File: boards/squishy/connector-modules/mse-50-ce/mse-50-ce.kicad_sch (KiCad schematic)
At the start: 14 parts, among them J1 SCSI PHY Mezz, J3 Conn_01x04, J5 Centronics 50, U1 M24C02-RMC

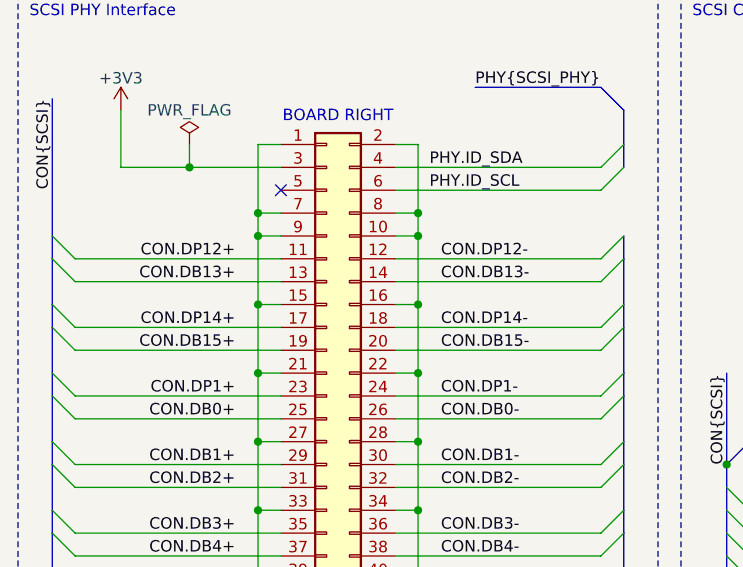
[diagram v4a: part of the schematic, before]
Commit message: squishy: connectors: s/DP12/DB12/g s/DP14/DB14/g
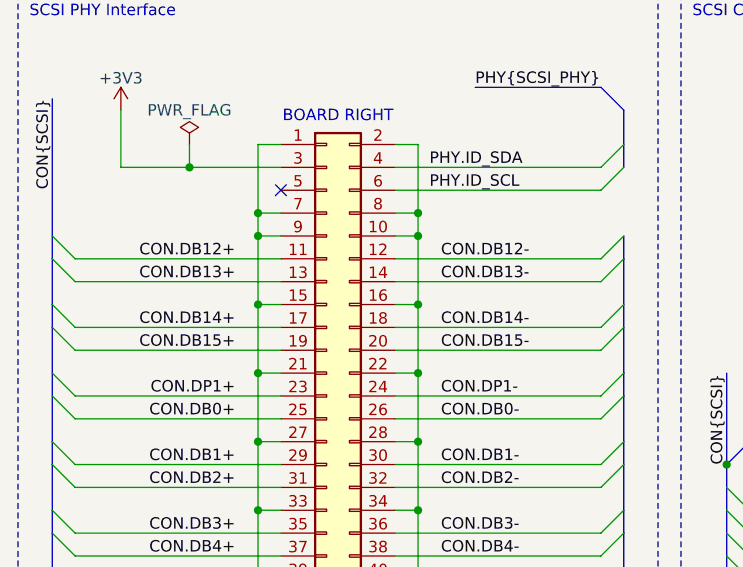
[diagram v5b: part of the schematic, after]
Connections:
- net CON.DP12+ renamed CON.DB12+
- net CON.DP12- renamed CON.DB12-
- net CON.DP14+ renamed CON.DB14+
- net CON.DP14- renamed CON.DB14-
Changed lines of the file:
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@@
 		)
 	)
-	(label "CON.DP14-"
+	(label "CON.DB14-"
 		(at 60.96 52.07 0)
 		(fields_autoplaced yes)
@@
 		)
 	)
-	(label "CON.DP12+"
+	(label "CON.DB12+"
 		(at 38.1 44.45 180)
 		(fields_autoplaced yes)
@@
 		)
 	)
-	(label "CON.DP12-"
+	(label "CON.DB12-"
 		(at 60.96 44.45 0)
 		(fields_autoplaced yes)
@@
 		)
 	)
-	(label "CON.DP14+"
+	(label "CON.DB14+"
 		(at 38.1 52.07 180)
 		(fields_autoplaced yes)

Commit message: squishy: connectors: updated SCSI connector metadata for mse-50-ce
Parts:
- J5: value Centronics 50 -> 112-050-213R001; MFR (none) -> NorComp; MPN (none) -> 112-050-213R001; URL (none) -> https://www.norcomp.net/series/112-series?search_part=112-0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
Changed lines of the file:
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@@
 			)
 		)
-		(property "Value" "Centronics 50"
-			(at 123.19 67.31 0)
+		(property "Value" "112-050-213R001"
+			(at 123.19 101.6 90)
 			(effects
 				(font
@@
 			)
 		)
-		(property "Datasheet" "~"
+		(property "Datasheet" "https://content.norcomp.net/rohspdfs/SCSI-050Ribbon/11Y/112/112-YYY-213RYY1.pdf"
 			(at 121.92 120.65 0)
 			(effects
@@
 			)
 		)
-		(property "Description" "Generic connector, double row, 02x25, counter clockwise pin numbering scheme (similar to DIP package numbering), with shielding"
+		(property "Description" "Centronics 50-pin Connector"
 			(at 123.19 101.6 0)
 			(effects
+				(font
+					(size 1.27 1.27)
+				)
+				(hide yes)
+			)
+		)
+		(property "MFR" "NorComp"
+			(at 123.19 101.6 0)
+			(effects
+				(font
+					(size 1.27 1.27)
+				)
+				(hide yes)
+			)
+		)
+		(property "MPN" "112-050-213R001"
+			(at 123.19 101.6 0)
+			(effects
+				(font
+					(size 1.27 1.27)
+				)
+				(hide yes)
+			)
+		)
+		(property "URL" "https://www.norcomp.net/series/112-series?search_part=112-050-213R001"
+			(at 123.19 101.6 0)
+			(effects

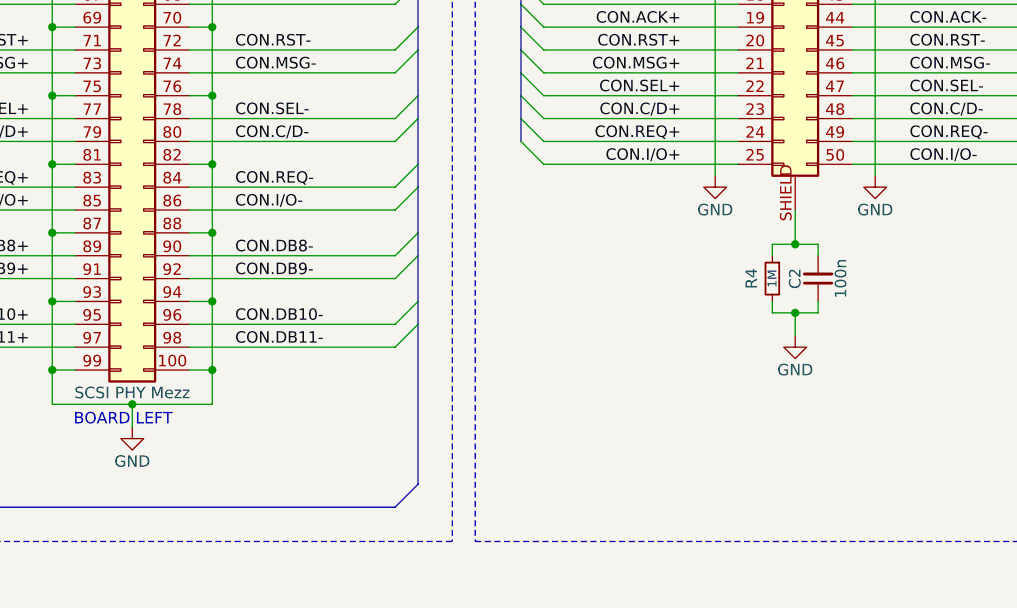
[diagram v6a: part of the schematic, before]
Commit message: squishy: connectors: cleaned up ERC on the mse-50-ce connector
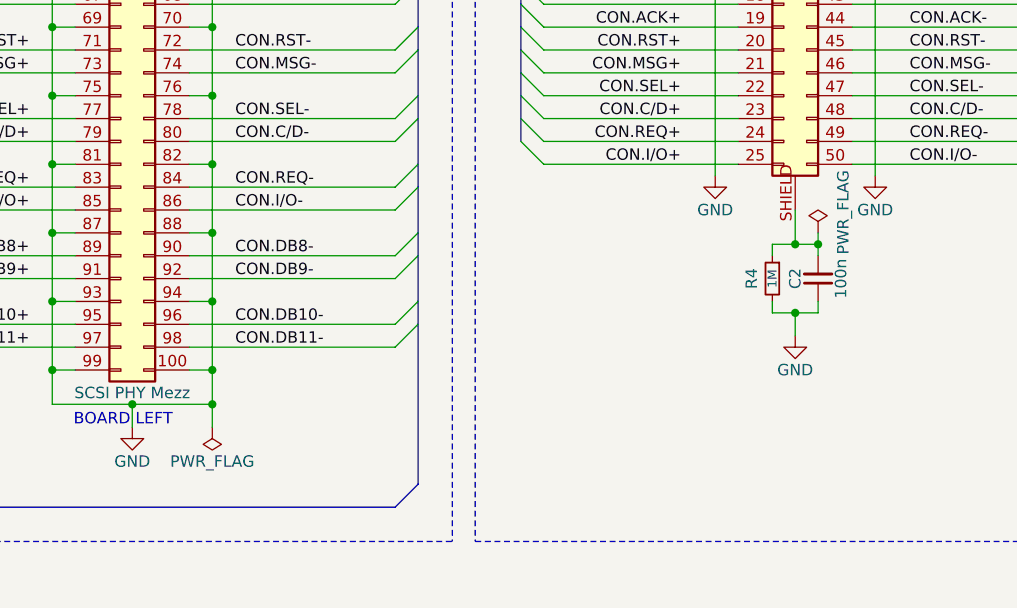
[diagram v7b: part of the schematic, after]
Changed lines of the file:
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@@
 	)
 	(junction
+		(at 125.73 142.24)
+		(diameter 0)
+		(color 0 0 0 0)
+	)
+	(junction
+		(at 58.42 160.02)
+		(diameter 0)
+		(color 0 0 0 0)
+	)
+	(junction
 		(at 58.42 41.91)
 		(diameter 0)
@@
 	(wire
 		(pts
+			(xy 125.73 140.97) (xy 125.73 142.24)
+		)
+		(stroke
+			(width 0)
+			(type default)
+		)
+	)
+	(wire
+		(pts
 			(xy 55.88 133.35) (xy 58.42 133.35)
 		)
@@
 	(wire
 		(pts
+			(xy 58.42 160.02) (xy 58.42 162.56)
+		)
+		(stroke
+			(width 0)
+			(type default)
+		)
+	)
+	(wire
+		(pts
 			(xy 40.64 57.15) (xy 40.64 64.77)
 		)
@@
 	)
 	(symbol
+		(lib_id "power:PWR_FLAG")
+		(at 58.42 162.56 180)
+		(unit 1)
+		(exclude_from_sim no)
+		(in_bom yes)
+		(on_board yes)
+		(dnp no)
+		(property "Reference" "#FLG02"
+			(at 58.42 164.465 0)
+			(effects
+				(font
+					(size 1.27 1.27)
+				)
+				(hide yes)
+			)
+		)
+		(property "Value" "PWR_FLAG"
+			(at 58.42 166.37 0)
+			(effects
+				(font
+					(size 1.27 1.27)
+				)
+			)
+		)
+		(property "Footprint" ""
+			(at 58.42 162.56 0)
+			(effects
+				(font
+					(size 1.27 1.27)
+				)
+				(hide yes)
+			)
+		)
+		(property "Datasheet" "~"
+			(at 58.42 162.56 0)
+			(effects
+				(font
+					(size 1.27 1.27)
+				)
+				(hide yes)
+			)
+		)
+		(property "Description" "Special symbol for telling ERC where power comes from"
+			(at 58.42 162.56 0)
+			(effects
+				(font
+					(size 1.27 1.27)
+				)
+				(hide yes)
+			)
+		)
+		(pin "1"
+		)
+		(instances
+			(project "mse-50-ce"
+				(path "/bd9eafec-5355-49e4-b2e3-916daacb0a86"
+					(reference "#FLG02")
+					(unit 1)
+				)
+			)
+		)
+	)
+	(symbol
 		(lib_id "power:GND")
 		(at 123.19 152.4 0)
@@
 					(unit 1)
 				)
+			)
+		)
+	)
+	(symbol
+		(lib_id "power:PWR_FLAG")
+		(at 125.73 140.97 0)
+		(unit 1)
+		(exclude_from_sim no)
+		(in_bom yes)
+		(on_board yes)
+		(dnp no)
+		(property "Reference" "#FLG03"
+			(at 125.73 139.065 0)
+			(effects
+				(font
+					(size 1.27 1.27)
+				)
+				(hide yes)
+			)
+		)
+		(property "Value" "PWR_FLAG"
+			(at 128.524 138.684 90)
+			(effects
+				(font
+					(size 1.27 1.27)
+				)
+			)
+		)
+		(property "Footprint" ""
+			(at 125.73 140.97 0)
+			(effects
+				(font
+					(size 1.27 1.27)
+				)
+				(hide yes)
+			)
+		)
+		(property "Datasheet" "~"
+			(at 125.73 140.97 0)
+			(effects
+				(font
+					(size 1.27 1.27)
+				)
+				(hide yes)
+			)
+		)
+		(property "Description" "Special symbol for telling ERC where power comes from"
+			(at 125.73 140.97 0)
+			(effects
+				(font
+					(size 1.27 1.27)
+				)
+				(hide yes)
+			)
+		)
+		(pin "1"
+		)
+		(instances
+			(project "mse-50-ce"
+				(path "/bd9eafec-5355-49e4-b2e3-916daacb0a86"
+					(reference "#FLG03")
+					(unit 1)
+				)

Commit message: squishy: connectors: updated part metadata on mse-50-ce prior to CAM generation
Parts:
- J3: now left out of the parts list
- J5: SUPPLIER (none) -> DigiKey; SUPPLIER_OC (none) -> 1050RFA-ND; SUPPLIER_URL (none) -> https://www.digikey.com/short/vt4vc8rp
- R4: MFR (none) -> Vishay Dale; MPN (none) -> CRCW06031M00FKEA; SUPPLIER_OC (none) -> 541-1.00MHDKR-ND; SUPPLIER_URL (none) -> https://www.digikey.com/short/18qqp0zw; Tolerance (none) -> ±1% 1/10W
- U1: MFR (none) -> STMicroelectronics; MPN (none) -> M24C02-RMC6TG; SUPPLIER (none) -> DigiKey; SUPPLIER_OC (none) -> 497-17822-1-ND; SUPPLIER_URL (none) -> https://www.digikey.com/short/r9drrzr3
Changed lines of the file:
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@@
 			)
 		)
-		(property "Datasheet" ""
+		(property "Datasheet" "https://www.vishay.com/docs/20035/dcrcwe3.pdf"
 			(at 120.65 146.05 0)
 			(effects
@@
 			)
 		)
-		(property "MFR" ""
+		(property "MFR" "Vishay Dale"
 			(at 120.65 146.05 90)
 			(effects
@@
 			)
 		)
-		(property "MPN" ""
+		(property "MPN" "CRCW06031M00FKEA"
 			(at 120.65 146.05 90)
 			(effects
@@
 			)
 		)
-		(property "Tolerance" ""
+		(property "Tolerance" "±1% 1/10W"
 			(at 120.65 146.05 0)
 			(effects
@@
 			)
 		)
-		(property "SUPPLIER_OC" ""
+		(property "SUPPLIER_OC" "541-1.00MHDKR-ND"
 			(at 120.65 146.05 0)
 			(effects
@@
 			)
 		)
-		(property "SUPPLIER_URL" ""
+		(property "SUPPLIER_URL" "https://www.digikey.com/short/18qqp0zw"
 			(at 120.65 146.05 0)
 			(effects
@@
 		(unit 1)
 		(exclude_from_sim no)
-		(in_bom yes)
+		(in_bom no)
 		(on_board yes)
 		(dnp no)
@@
 		)
 		(property "URL" "https://www.norcomp.net/series/112-series?search_part=112-050-213R001"
+			(at 123.19 101.6 0)
+			(effects
+				(font
+					(size 1.27 1.27)
+				)
+				(hide yes)
+			)
+		)
+		(property "SUPPLIER" "DigiKey"
+			(at 123.19 101.6 0)
+			(effects
+				(font
+					(size 1.27 1.27)
+				)
+				(hide yes)
+			)
+		)
+		(property "SUPPLIER_OC" "1050RFA-ND"
+			(at 123.19 101.6 0)
+			(effects
+				(font
+					(size 1.27 1.27)
+				)
+				(hide yes)
+			)
+		)
+		(property "SUPPLIER_URL" "https://www.digikey.com/short/vt4vc8rp"
 			(at 123.19 101.6 0)
 			(effects
@@
 			(at 238.76 147.32 0)
 			(effects
+				(font
+					(size 1.27 1.27)
+				)
+				(hide yes)
+			)
+		)
+		(property "MFR" "STMicroelectronics"
+			(at 238.76 147.32 0)
+			(effects
+				(font
+					(size 1.27 1.27)
+				)
+				(hide yes)
+			)
+		)
+		(property "MPN" "M24C02-RMC6TG"
+			(at 238.76 147.32 0)
+			(effects
+				(font
+					(size 1.27 1.27)
+				)
+				(hide yes)
+			)
+		)
+		(property "SUPPLIER" "DigiKey"
+			(at 238.76 147.32 0)
+			(effects
+				(font
+					(size 1.27 1.27)
+				)
+				(hide yes)
+			)
+		)
+		(property "SUPPLIER_OC" "497-17822-1-ND"
+			(at 238.76 147.32 0)
+			(effects
+				(font
+					(size 1.27 1.27)
+				)
+				(hide yes)
+			)
+		)
+		(property "SUPPLIER_URL" "https://www.digikey.com/short/r9drrzr3"
+			(at 238.76 147.32 0)
+			(effects
